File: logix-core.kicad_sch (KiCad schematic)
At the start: 0 parts

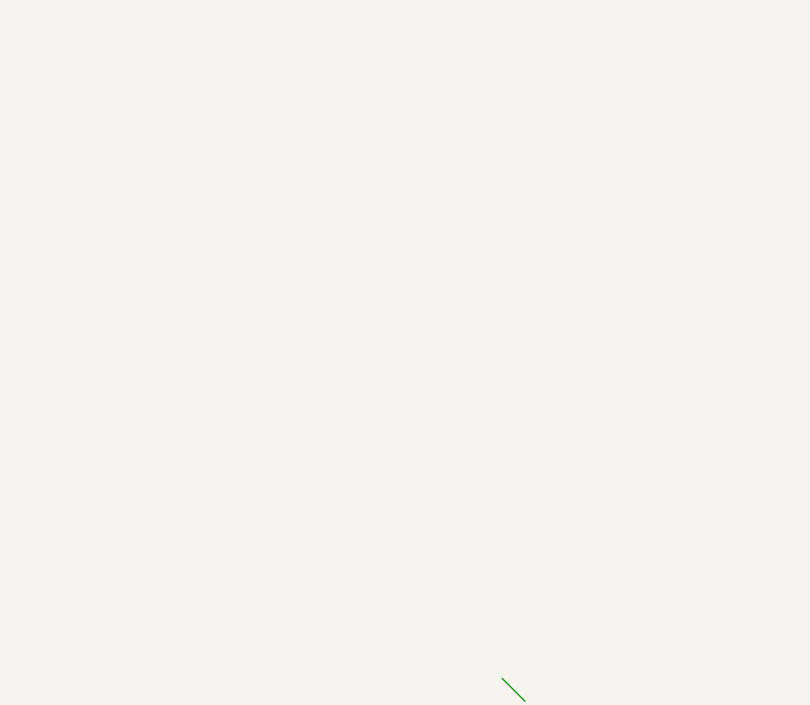
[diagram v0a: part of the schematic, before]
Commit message: filled out back connector, finished ddr pinning according to vivado
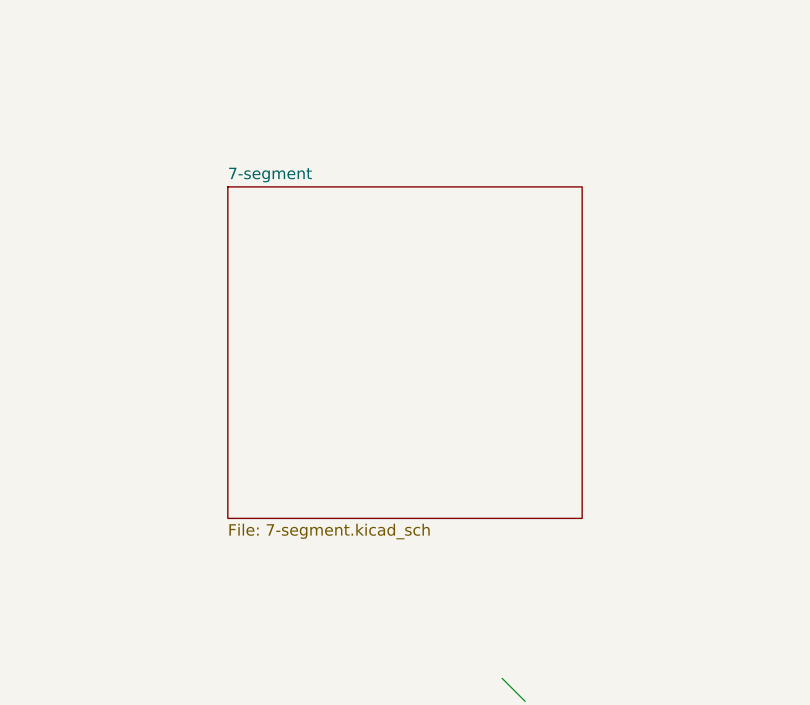
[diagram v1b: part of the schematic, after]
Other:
- added sheet 7-segment (7-segment.kicad_sch)
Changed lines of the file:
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@@
+	)
+	(sheet
+		(at 152.4 38.1)
+		(size 39.37 36.83)
+		(exclude_from_sim no)
+		(in_bom yes)
+		(on_board yes)
+		(dnp no)
+		(fields_autoplaced yes)
+		(stroke
+			(width 0.1524)
+			(type solid)
+		)
+		(fill
+			(color 0 0 0 0.0000)
+		)
+		(property "Sheetname" "7-segment"
+			(at 152.4 37.3884 0)
+			(effects
+				(font
+					(size 1.27 1.27)
+				)
+				(justify left bottom)
+			)
+		)
+		(property "Sheetfile" "7-segment.kicad_sch"
+			(at 152.4 75.5146 0)
+			(effects
+				(font
+					(size 1.27 1.27)
+				)
+				(justify left top)
+			)
+		)
+		(instances
+			(project "logix-core"
+				(path "/cf3b7c5f-6ddc-4e3f-9529-0bcf5eec6f23"
+					(page "15")
+				)
+			)
+		)
 	)
 	(sheet

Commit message: added a lot of stuff
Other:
- sheet 7-segment renamed 7SEG1
- added sheet 7SEG2 (7-segment.kicad_sch)
- added sheet 7SEG3 (7-segment.kicad_sch)
- added sheet DIP_SWITCH (dip_switch.kicad_sch)
- sheet 7SEG1 ports: added 7SEG_A, 7SEG_C; removed none
- sheet Backend Connector ports: added I2C, INT#, PCIE, SERIAL, SPARE; removed none
- sheet FPGA ports: added 7SEG1_A, 7SEG1_C, 7SEG2_A, 7SEG2_C, 7SEG3_A, 7SEG3_C, BACK_I2C, BACK_INT#, BACK_PCIE, BACK_SERIAL, BACK_SPARE, BTN1#, BTN2#, DIP_SW, FRONT_I2C, FRONT_INT#, RST_BTN#; removed none
- sheet Frontend Connector ports: added I2C, INT#; removed none
- sheet SPI Flash ports: added FLASH_SPI; removed none
- sheet USB ports: added UART; removed none

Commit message: more floorplanning
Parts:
- added FID1, FID2, FID3, FID4: Fiducial, Fiducial:Fiducial_0.5mm_Mask1mm, symbol Mechanical:Fiducial
- added H10, H11, H12, H9: MountingHole_Pad, MountingHole:MountingHole_3.2mm_M3_DIN965_Pad, symbol Mechanical:MountingHole_Pad
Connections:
- new net GND: H10.1, H11.1, H12.1, H9.1
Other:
- sheet FPGA ports: added FLASH_SPI; removed none
